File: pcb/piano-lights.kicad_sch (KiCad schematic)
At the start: 38 parts, among them J1 USB-C 6-Pin, J2 FTDI RS232, J3 LED Strip, J4 AVR-ISP-6, J5 MIDI IN, J6 MIDI THRU, J7 MIDI Coupler B, J8 MIDI Coupler A, SW1 Button, SW2 Reset, U1 ATmega328, U2 H11L1, U3 74AHC1G125, Y1 16MHz

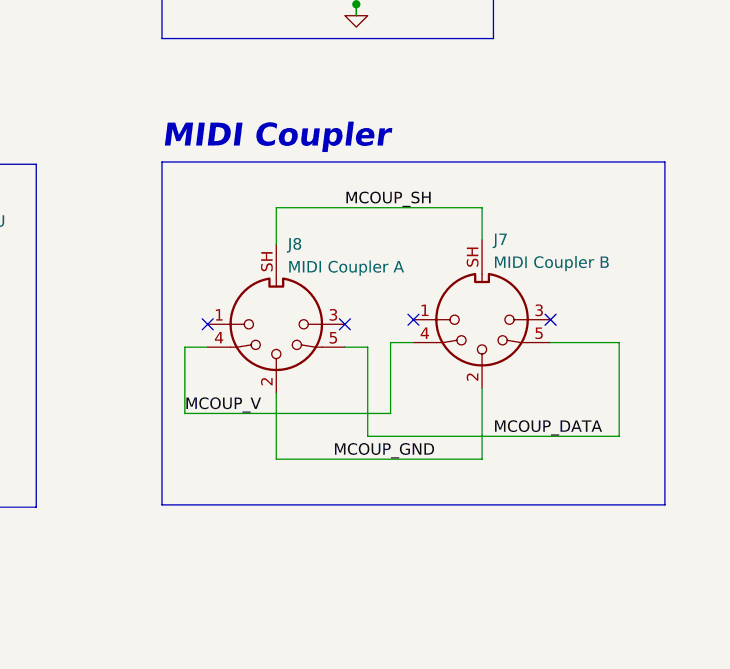
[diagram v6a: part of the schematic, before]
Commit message: Clean up MIDI coupler schematic a bit
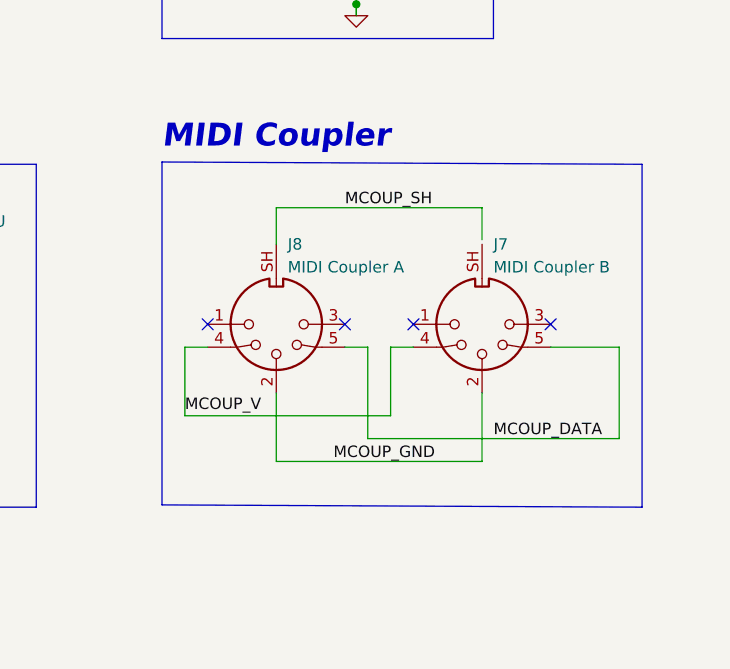
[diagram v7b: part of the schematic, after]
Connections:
- net MCOUP_SH: no longer J7.SH
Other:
- moved on the sheet: J7
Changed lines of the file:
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@@
   (no_connect (at 212.09 144.78))
   (no_connect (at 130.81 83.82))
-  (no_connect (at 219.71 144.272))
+  (no_connect (at 219.71 144.78))
   (no_connect (at 97.79 99.06))
   (no_connect (at 130.81 104.14))
   (no_connect (at 130.81 91.44))
   (no_connect (at 130.81 81.28))
-  (no_connect (at 234.95 144.272))
+  (no_connect (at 234.95 144.78))
   (no_connect (at 130.81 63.5))
   (no_connect (at 130.81 101.6))
@@
     (stroke (width 0) (type default) (color 0 0 0 0))
   )
-  (wire (pts (xy 204.47 152.4) (xy 204.47 159.766))
+  (wire (pts (xy 204.47 152.4) (xy 204.47 160.02))
     (stroke (width 0) (type default) (color 0 0 0 0))
   )
@@
     (stroke (width 0) (type default) (color 0 0 0 0))
   )
-  (wire (pts (xy 217.17 146.812) (xy 219.71 146.812))
+  (wire (pts (xy 217.17 147.32) (xy 219.71 147.32))
     (stroke (width 0) (type default) (color 0 0 0 0))
   )
@@
     (stroke (width 0) (type default) (color 0 0 0 0))
   )
-  (wire (pts (xy 242.57 146.812) (xy 234.95 146.812))
+  (wire (pts (xy 242.57 147.32) (xy 234.95 147.32))
     (stroke (width 0) (type default) (color 0 0 0 0))
   )
@@
     (stroke (width 0) (type default) (color 0 0 0 0))
   )
-  (polyline (pts (xy 191.77 126.746) (xy 247.65 126.746))
+  (polyline (pts (xy 191.77 126.746) (xy 245.11 127))
     (stroke (width 0) (type default) (color 0 0 0 0))
   )
@@
     (stroke (width 0) (type default) (color 0 0 0 0))
   )
-  (polyline (pts (xy 247.65 164.846) (xy 247.65 126.746))
+  (polyline (pts (xy 245.11 165.1) (xy 245.11 127))
     (stroke (width 0) (type default) (color 0 0 0 0))
   )
@@
     (stroke (width 0) (type default) (color 0 0 0 0))
   )
-  (wire (pts (xy 242.57 157.226) (xy 242.57 146.812))
+  (wire (pts (xy 242.57 157.48) (xy 242.57 147.32))
     (stroke (width 0) (type default) (color 0 0 0 0))
   )
@@
     (stroke (width 0) (type default) (color 0 0 0 0))
   )
+  (wire (pts (xy 227.33 152.4) (xy 227.33 160.02))
+    (stroke (width 0) (type default) (color 0 0 0 0))
+  )
   (wire (pts (xy 196.85 147.32) (xy 194.31 147.32))
     (stroke (width 0) (type default) (color 0 0 0 0))
   )
-  (wire (pts (xy 194.31 154.686) (xy 217.17 154.686))
+  (wire (pts (xy 194.31 154.94) (xy 217.17 154.94))
     (stroke (width 0) (type default) (color 0 0 0 0))
   )
@@
     (stroke (width 0) (type default) (color 0 0 0 0))
   )
-  (wire (pts (xy 194.31 147.32) (xy 194.31 154.686))
+  (wire (pts (xy 194.31 147.32) (xy 194.31 154.94))
     (stroke (width 0) (type default) (color 0 0 0 0))
   )
@@
     (stroke (width 0) (type default) (color 0 0 0 0))
   )
-  (wire (pts (xy 217.17 154.686) (xy 217.17 146.812))
+  (wire (pts (xy 217.17 154.94) (xy 217.17 147.32))
     (stroke (width 0) (type default) (color 0 0 0 0))
   )
@@
     (stroke (width 0) (type default) (color 0 0 0 0))
   )
-  (wire (pts (xy 204.47 159.766) (xy 227.33 159.766))
+  (wire (pts (xy 204.47 160.02) (xy 227.33 160.02))
     (stroke (width 0) (type default) (color 0 0 0 0))
   )
@@
     (stroke (width 0) (type default) (color 0 0 0 0))
   )
-  (wire (pts (xy 214.63 147.32) (xy 214.63 157.226))
+  (wire (pts (xy 214.63 147.32) (xy 214.63 157.48))
     (stroke (width 0) (type default) (color 0 0 0 0))
   )
@@
     (stroke (width 0) (type default) (color 0 0 0 0))
   )
-  (polyline (pts (xy 191.77 164.846) (xy 247.65 164.846))
+  (polyline (pts (xy 191.77 164.846) (xy 245.11 165.1))
     (stroke (width 0) (type default) (color 0 0 0 0))
   )
@@
     (stroke (width 0) (type default) (color 0 0 0 0))
   )
-  (wire (pts (xy 227.33 159.766) (xy 227.33 151.892))
-    (stroke (width 0) (type default) (color 0 0 0 0))
-  )
   (polyline (pts (xy 45.72 198.12) (xy 45.72 184.15))
     (stroke (width 0) (type default) (color 0 0 0 0))
@@
     (stroke (width 0) (type default) (color 0 0 0 0))
   )
-  (wire (pts (xy 214.63 157.226) (xy 242.57 157.226))
+  (wire (pts (xy 214.63 157.48) (xy 242.57 157.48))
     (stroke (width 0) (type default) (color 0 0 0 0))
   )
@@
     (effects (font (size 1.27 1.27)) (justify left bottom))
   )
-  (label "MCOUP_DATA" (at 228.6 157.226 0)
+  (label "MCOUP_DATA" (at 228.6 157.48 0)
     (effects (font (size 1.27 1.27)) (justify left bottom))
   )
@@
     (effects (font (size 1.27 1.27)) (justify left bottom))
   )
-  (label "MCOUP_GND" (at 210.82 159.766 0)
+  (label "MCOUP_GND" (at 210.82 160.02 0)
     (effects (font (size 1.27 1.27)) (justify left bottom))
   )
@@
     (pin "1")
   )
-  (symbol (lib_id "00-piano-lights:DIN-5_180degree_Shielded") (at 227.33 144.272 0) (mirror x) (unit 1)
-    (in_bom yes) (on_board yes)
-    (property "Reference" "J7" (id 0) (at 228.6 135.382 0)
+  (symbol (lib_id "00-piano-lights:DIN-5_180degree_Shielded") (at 227.33 144.78 0) (mirror x) (unit 1)
+    (in_bom yes) (on_board yes)
+    (property "Reference" "J7" (id 0) (at 228.6 135.89 0)
       (effects (font (size 1.27 1.27)) (justify left))
     )
-    (property "Value" "MIDI Coupler B" (id 1) (at 228.6 137.922 0)
+    (property "Value" "MIDI Coupler B" (id 1) (at 228.6 138.43 0)
       (effects (font (size 1.27 1.27)) (justify left))
     )
-    (property "Footprint" "00-Vendor_SDS-50J:CUI_SDS-50J" (id 2) (at 227.33 144.272 0)
-      (effects (font (size 1.27 1.27)) hide)
-    )
-    (property "Datasheet" "http://www.mouser.com/ds/2/18/40_c091_abd_e-75918.pdf" (id 3) (at 227.33 144.272 0)
-      (effects (font (size 1.27 1.27)) hide)
-    )
-    (property "Mfr" "CUI" (id 4) (at 227.33 144.272 0)
-      (effects (font (size 1.27 1.27)) hide)
-    )
-    (property "Mfr Part" "SDS-50J" (id 5) (at 227.33 144.272 0)
-      (effects (font (size 1.27 1.27)) hide)
-    )
-    (property "Vendor" "https://www.digikey.com/short/qh7jzdb5" (id 6) (at 227.33 144.272 0)
-      (effects (font (size 1.27 1.27)) hide)
-    )
+    (property "Footprint" "00-Vendor_SDS-50J:CUI_SDS-50J" (id 2) (at 227.33 144.78 0)
+      (effects (font (size 1.27 1.27)) hide)
+    )
+    (property "Datasheet" "http://www.mouser.com/ds/2/18/40_c091_abd_e-75918.pdf" (id 3) (at 227.33 144.78 0)
+      (effects (font (size 1.27 1.27)) hide)
+    )
+    (property "Mfr" "CUI" (id 4) (at 227.33 144.78 0)
+      (effects (font (size 1.27 1.27)) hide)
+    )
+    (property "Mfr Part" "SDS-50J" (id 5) (at 227.33 144.78 0)
+      (effects (font (size 1.27 1.27)) hide)
+    )
+    (property "Vendor" "https://www.digikey.com/short/qh7jzdb5" (id 6) (at 227.33 144.78 0)
+      (effects (font (size 1.27 1.27)) hide)
+    )

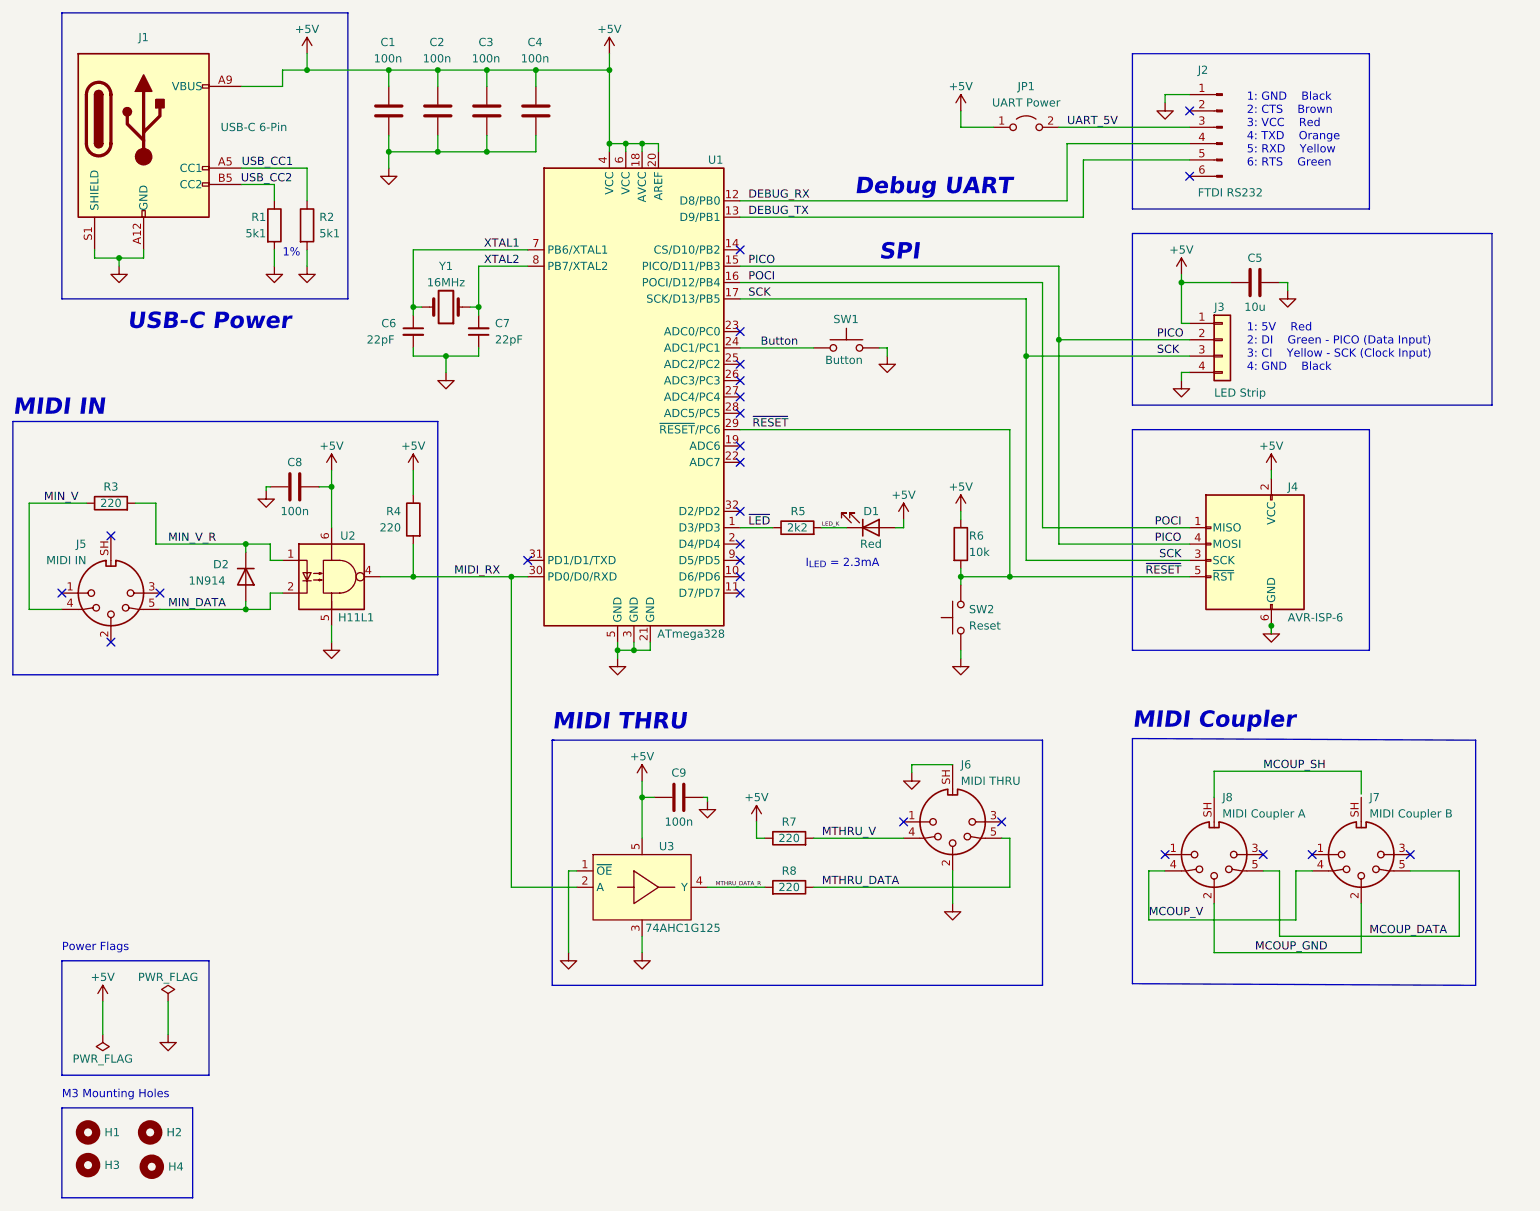
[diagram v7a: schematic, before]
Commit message: Clean up ERC and DRC issues
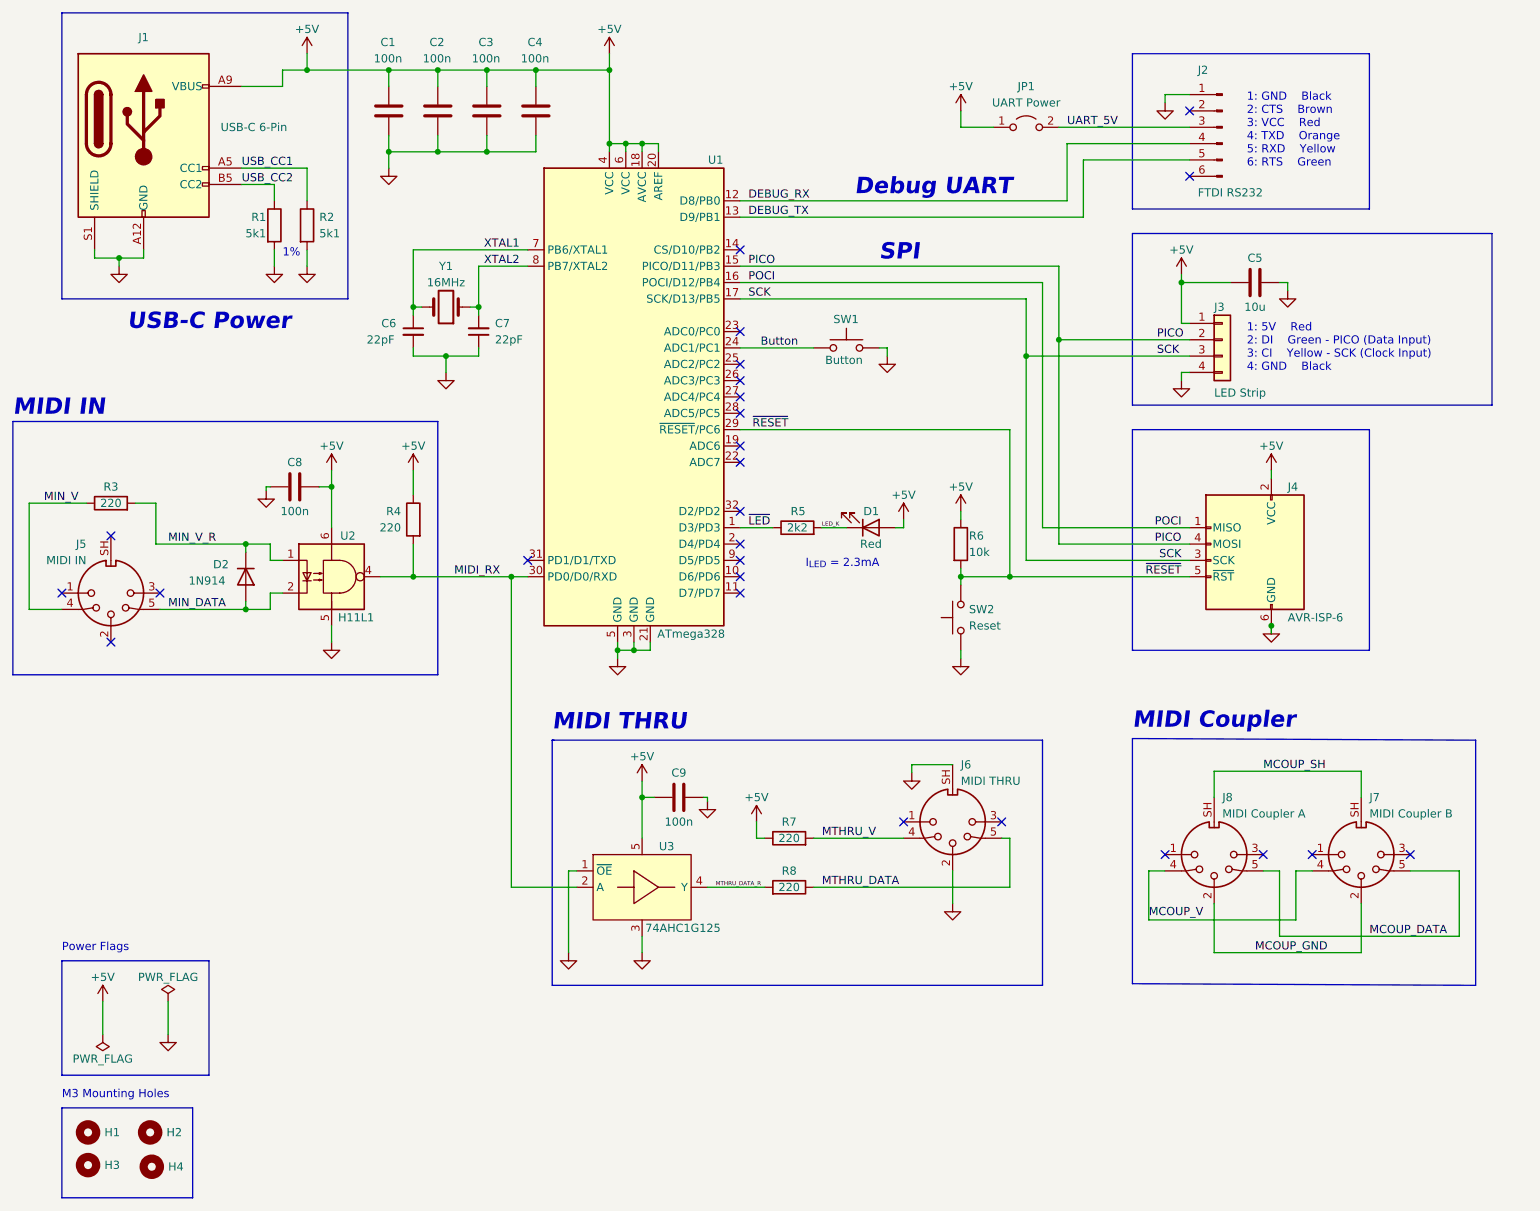
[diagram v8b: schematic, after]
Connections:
- net MCOUP_SH: now also J7.SH
- net USB_CC2: now also J1.B5 (CC2), R1.1
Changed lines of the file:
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@@
     (stroke (width 0) (type default) (color 0 0 0 0))
   )
-  (wire (pts (xy 227.33 131.826) (xy 227.33 135.382))
+  (wire (pts (xy 227.33 131.826) (xy 227.33 135.89))
     (stroke (width 0) (type default) (color 0 0 0 0))
   )
@@
     (effects (font (size 1.27 1.27)) (justify left bottom))
   )
-  (label "USB_CC2" (at 53.213 40.64 0)
-    (effects (font (size 1.27 1.27)) (justify left bottom))
-  )
+  (label "USB_CC2" (at 53.34 40.64 0)
+    (effects (font (size 1.27 1.27)) (justify left bottom))
+  )
